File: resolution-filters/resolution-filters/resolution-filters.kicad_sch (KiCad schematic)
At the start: 64 parts, among them J501 Conn_Coaxial, J502 Conn_Coaxial, J503 Terminal Block, K501 G5V-1, K502 G5V-1, SW501 SW_SPST, T501 Transformer_1P_1S, T502 Transformer_1P_1S, Y501 10.7MHz, Y502 10.7MHz, Y503 10.7MHz, Y504 10.7MHz

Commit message: resolution-filters.kicad_pcb updated
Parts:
- renumbered TP106 to TP506
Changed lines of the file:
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@@
   (symbol (lib_id "Connector:TestPoint_Probe") (at 248.92 139.7 0) (unit 1)
     (in_bom yes) (on_board yes)
-    (property "Reference" "TP106" (id 0) (at 247.65 134.62 0)
+    (property "Reference" "TP506" (id 0) (at 247.65 134.62 0)
       (effects (font (size 1.27 1.27)) (justify left))
     )
@@
       (reference "T502") (unit 1) (value "Transformer_1P_1S") (footprint "Transformer_THT:Transformer_Toroid_Horizontal_D14.0mm_Amidon-T50")
     )
-    (path "/2853c34b-984d-44d8-ba16-62d0c554a1d2"
-      (reference "TP106") (unit 1) (value "TestPoint") (footprint "TestPoint:TestPoint_Pad_D2.0mm")
-    )
     (path "/55b937a5-a069-41a7-a6cd-6eb20147a4cb"
       (reference "TP501") (unit 1) (value "TestPoint") (footprint "TestPoint:TestPoint_Pad_D2.0mm")
@@
       (reference "TP505") (unit 1) (value "TestPoint") (footprint "TestPoint:TestPoint_Pad_D2.0mm")
     )
+    (path "/2853c34b-984d-44d8-ba16-62d0c554a1d2"
+      (reference "TP506") (unit 1) (value "TestPoint") (footprint "TestPoint:TestPoint_Pad_D2.0mm")
+    )
     (path "/95c07863-759b-434d-bbc4-10e35dd940f5"

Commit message: resolution-filters updates
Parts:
- T501, T502: symbol Device:Transformer_1P_1S -> resolution-filters:Transformer_1P_1S
- Y501, Y502, Y503, Y504: symbol Device:Crystal_GND3_Small -> resolution-filters:Crystal_GND3_Small
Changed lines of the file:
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@@
     (pin "1")
   )
-  (symbol (lib_id "Device:Transformer_1P_1S") (at 227.33 102.87 0) (mirror y) (unit 1)
+  (symbol (lib_id "resolution-filters:Transformer_1P_1S") (at 227.33 102.87 0) (mirror y) (unit 1)
     (in_bom yes) (on_board yes) (fields_autoplaced)
     (property "Reference" "T502" (id 0) (at 227.3173 92.71 0))
@@
     (pin "1")
   )
-  (symbol (lib_id "Device:Crystal_GND3_Small") (at 172.72 104.14 0) (mirror y) (unit 1)
+  (symbol (lib_id "resolution-filters:Crystal_GND3_Small") (at 172.72 104.14 0) (mirror y) (unit 1)
     (in_bom yes) (on_board yes)
     (property "Reference" "Y503" (id 0) (at 172.72 95.885 0))
@@
     (pin "1")
   )
-  (symbol (lib_name "Transformer_1P_1S_1") (lib_id "Device:Transformer_1P_1S") (at 48.26 102.87 0) (unit 1)
+  (symbol (lib_id "resolution-filters:Transformer_1P_1S") (at 48.26 102.87 0) (unit 1)
     (in_bom yes) (on_board yes) (fields_autoplaced)
     (property "Reference" "T501" (id 0) (at 48.2727 92.71 0))
@@
     (pin "1")
   )
-  (symbol (lib_id "Device:Crystal_GND3_Small") (at 198.12 104.14 0) (unit 1)
+  (symbol (lib_id "resolution-filters:Crystal_GND3_Small") (at 198.12 104.14 0) (unit 1)
     (in_bom yes) (on_board yes)
     (property "Reference" "Y504" (id 0) (at 198.12 95.885 0))
@@
     (pin "9")
   )
-  (symbol (lib_id "Device:Crystal_GND3_Small") (at 102.87 102.87 0) (unit 1)
+  (symbol (lib_id "resolution-filters:Crystal_GND3_Small") (at 102.87 102.87 0) (unit 1)
     (in_bom yes) (on_board yes)
     (property "Reference" "Y502" (id 0) (at 102.87 93.345 0))
@@
     (pin "1")
   )
-  (symbol (lib_id "Device:Crystal_GND3_Small") (at 77.47 102.87 0) (mirror y) (unit 1)
+  (symbol (lib_id "resolution-filters:Crystal_GND3_Small") (at 77.47 102.87 0) (mirror y) (unit 1)
     (in_bom yes) (on_board yes)
     (property "Reference" "Y501" (id 0) (at 77.47 93.345 0))

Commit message: resolution-filters - one more fix
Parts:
- J503: footprint resolution-filters:691137710002 -> 691137710002; symbol 691137710002:691137710002 -> resolution-filters:691137710002
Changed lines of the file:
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@@
     (pin "2")
   )
-  (symbol (lib_id "691137710002:691137710002") (at 138.43 16.51 0) (unit 1)
+  (symbol (lib_id "resolution-filters:691137710002") (at 138.43 16.51 0) (unit 1)
     (in_bom yes) (on_board yes)
     (property "Reference" "J503" (id 0) (at 137.16 15.24 0))
     (property "Value" "Terminal Block" (id 1) (at 147.32 17.145 0))
-    (property "Footprint" "resolution-filters:691137710002" (id 2) (at 138.43 16.51 0)
+    (property "Footprint" "691137710002" (id 2) (at 138.43 16.51 0)
       (effects (font (size 1.27 1.27)) (justify left bottom) hide)
     )
@@
     )
     (path "/408d2020-2238-45ff-98cc-145d953d5d62"
-      (reference "J503") (unit 1) (value "Terminal Block") (footprint "resolution-filters:691137710002")
+      (reference "J503") (unit 1) (value "Terminal Block") (footprint "691137710002")
     )
     (path "/bb707a19-9f15-45f6-9d84-f498055bcc3f"

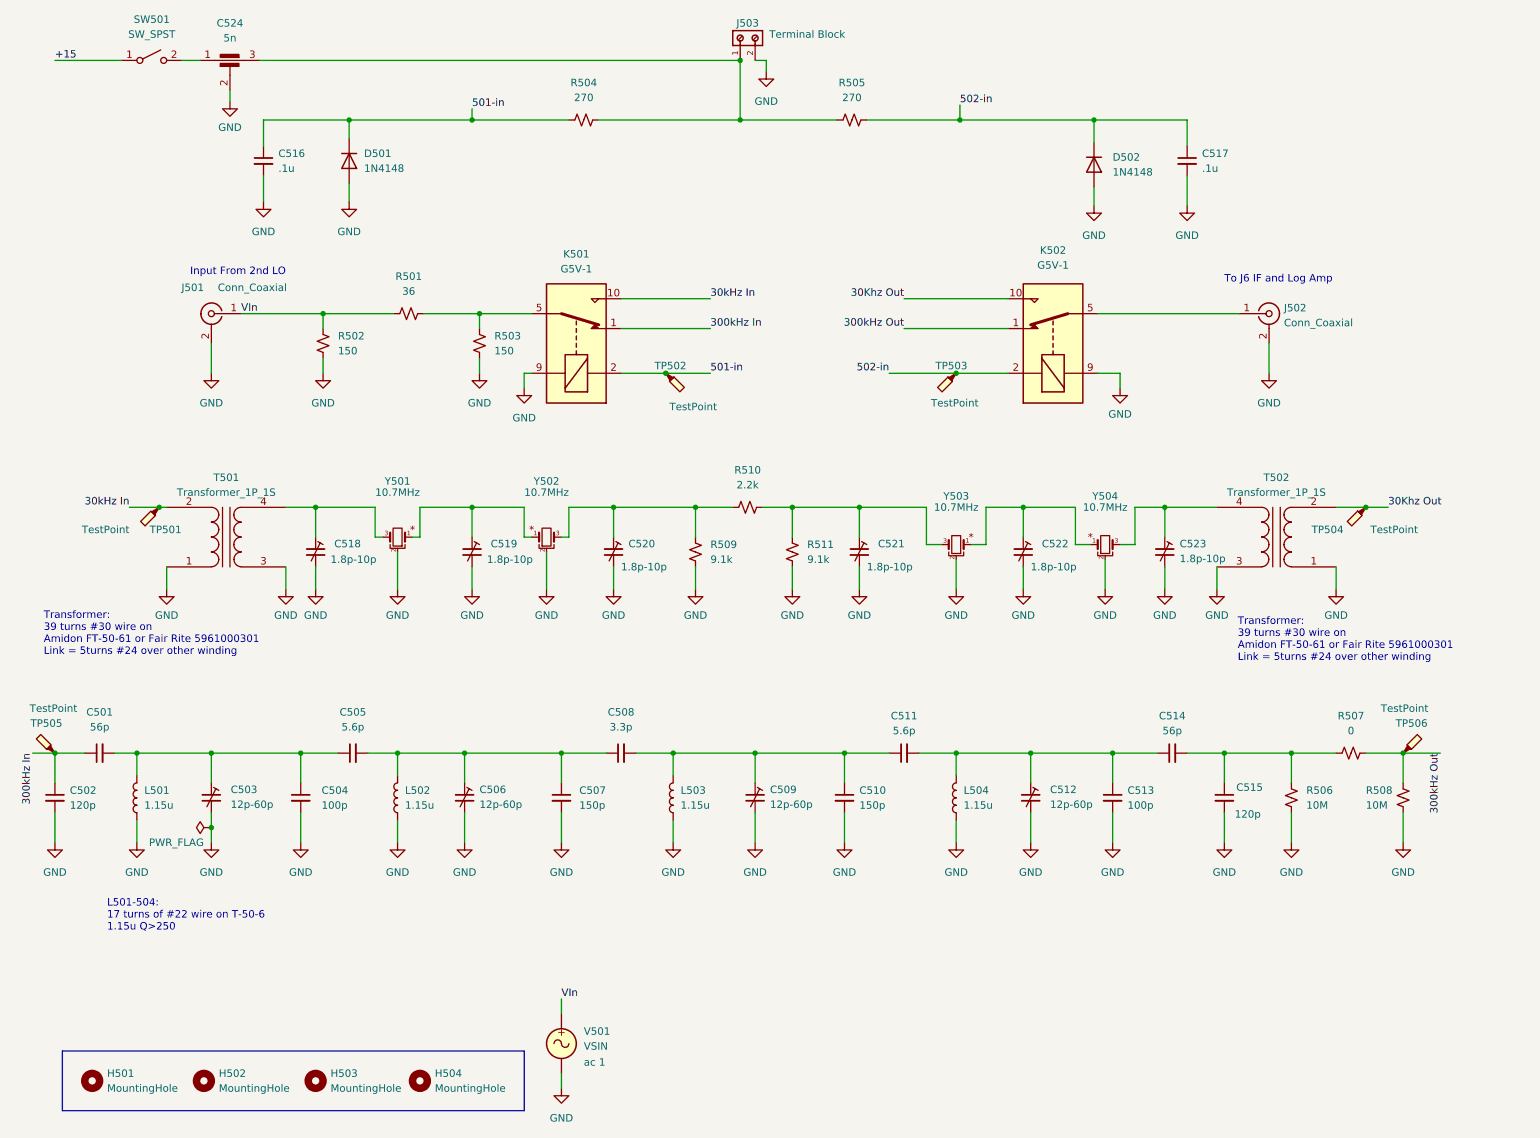
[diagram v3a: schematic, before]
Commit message: spice model for resolution-filters
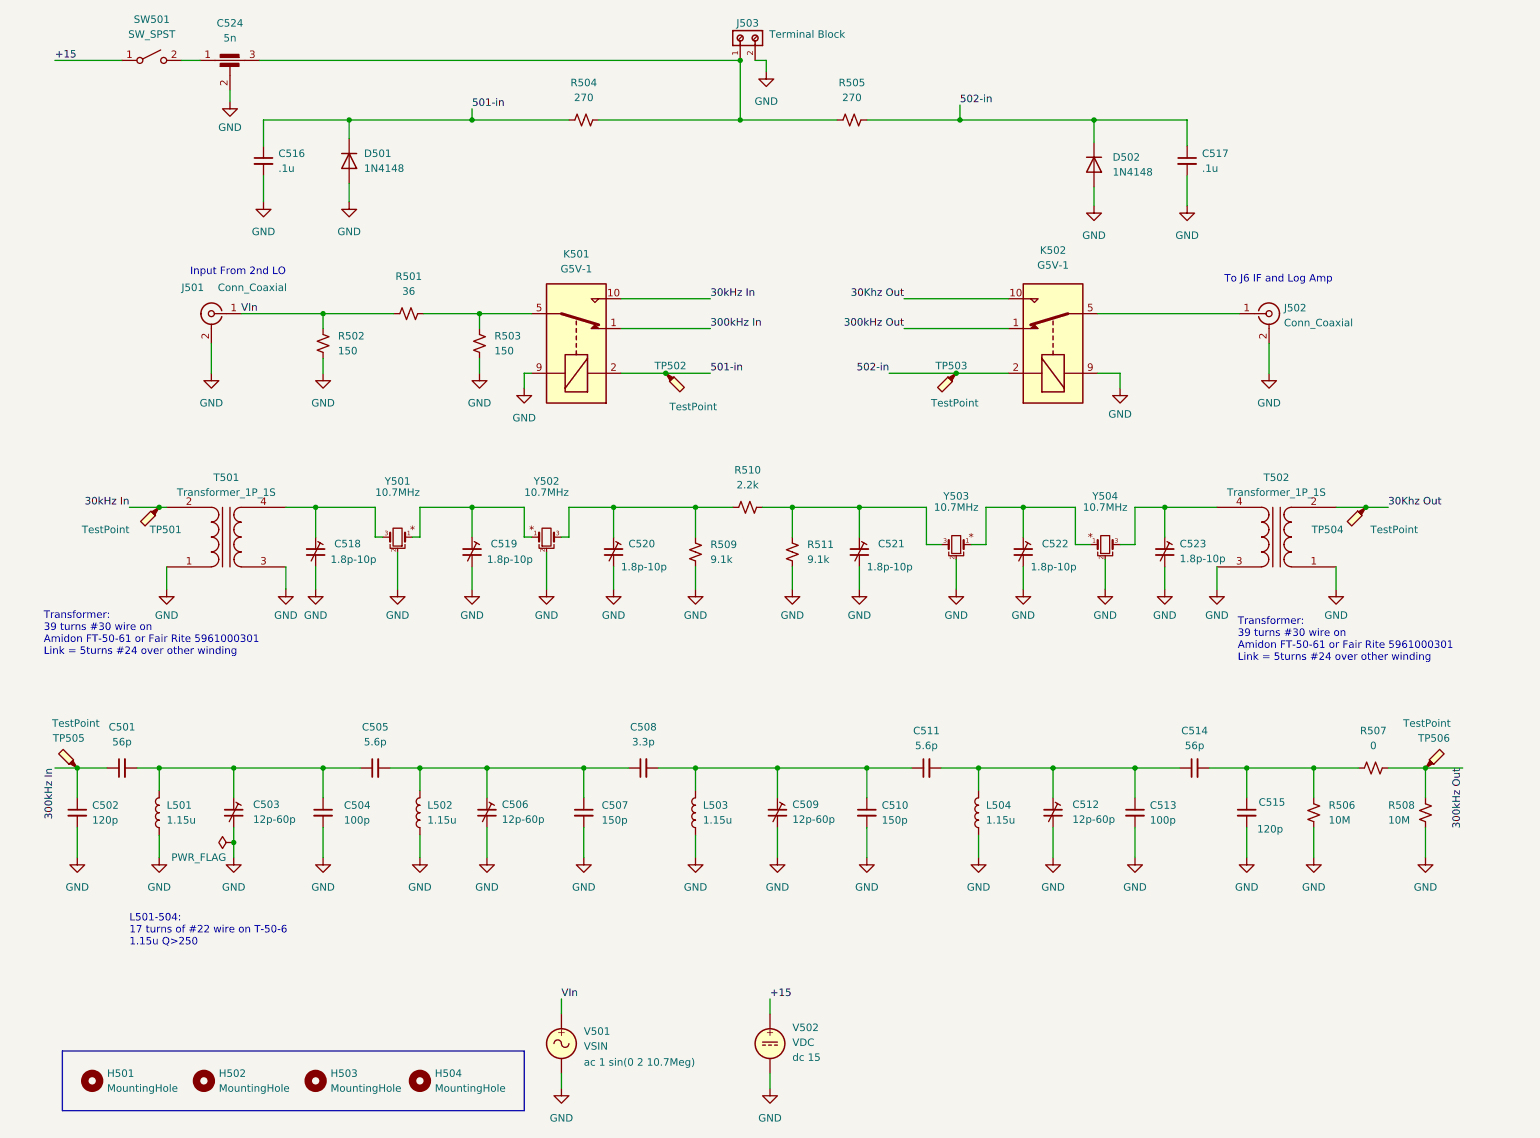
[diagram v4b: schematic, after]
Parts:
- added V502: VDC, symbol Simulation_SPICE:VDC
- V501: Spice_Model ac 1 -> ac 1 sin(0 2 10.7Meg)
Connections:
- net +15: now also V502.1
- net GND: now also V502.2
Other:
- moved on the sheet: C501, C502, C503, C504, C505, C506, C507, C508, C509, C510, C511, C512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
